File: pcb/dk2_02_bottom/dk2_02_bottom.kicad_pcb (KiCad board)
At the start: 2 copper layers, 120 x 80 mm, 76 parts, among them J1 Conn_01x18_Pin, J2 Conn_01x18_Pin, J3 Eurorack_Power, Q1 MMBT3904, U1 Pico, U2 AP7333-33SRG, U3 TL072, U4 PCM5102, U5 TL072, U6 TL072, U7 TL072, U8 XL1509-5.0

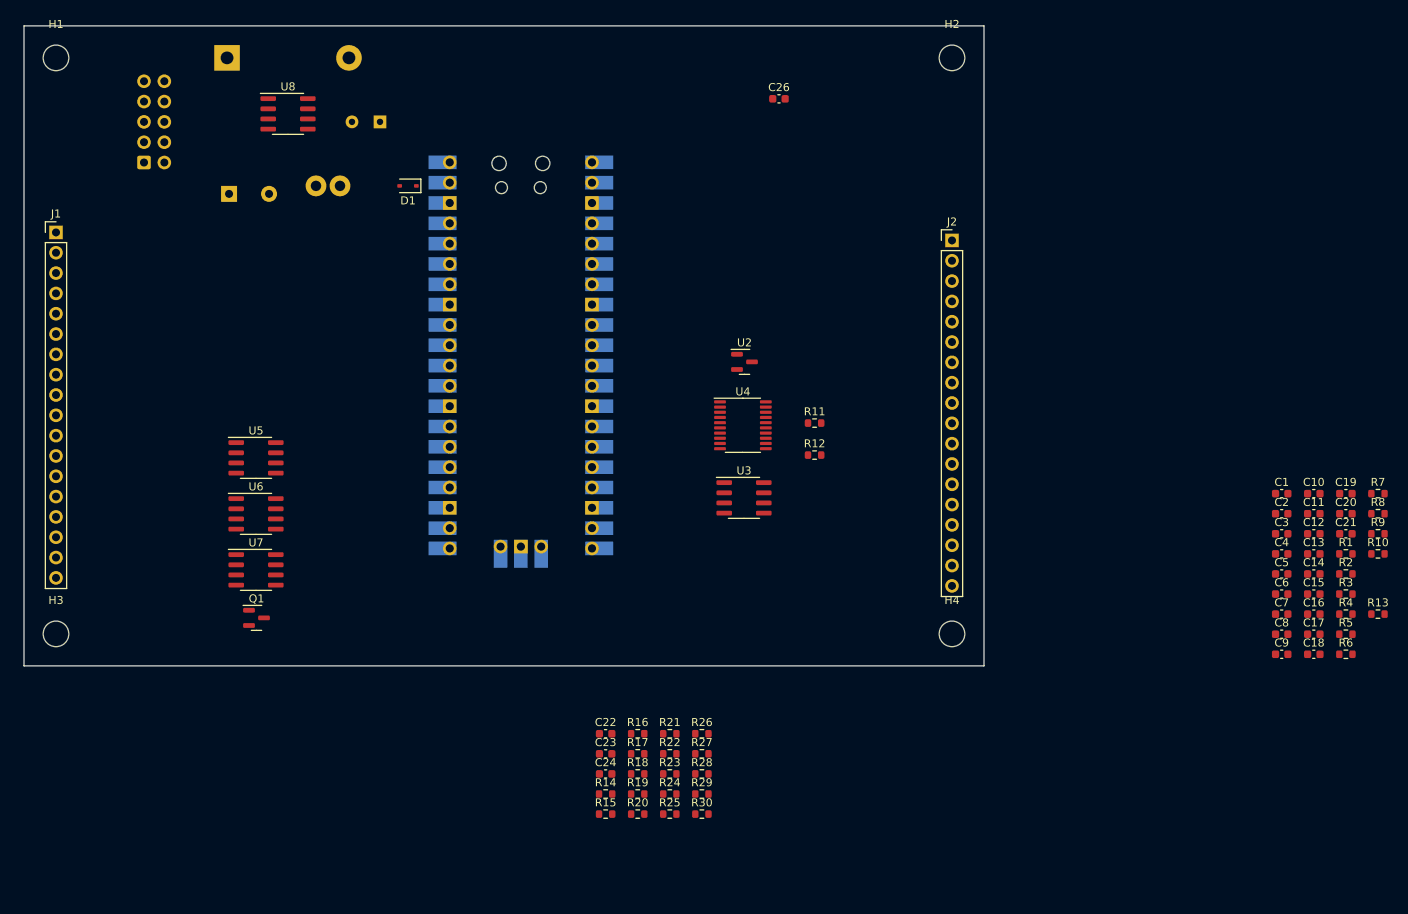
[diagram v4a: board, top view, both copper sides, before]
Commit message: started component placement on bottom board
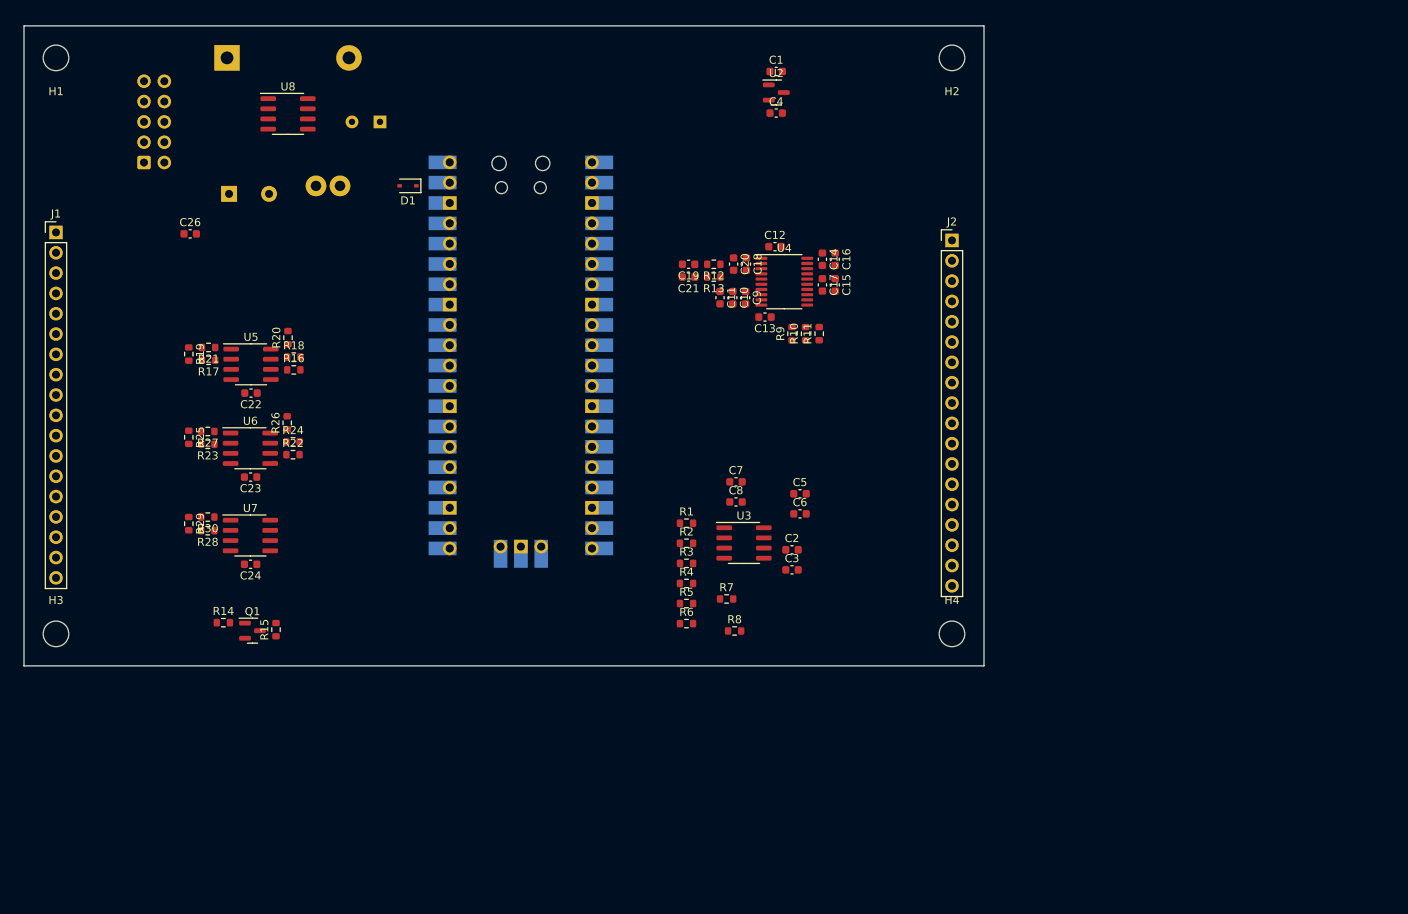
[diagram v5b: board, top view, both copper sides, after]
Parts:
- moved R13 93.1 mm to (166.2, 81.4), turned to 180 degrees
- moved C21 88.2 mm to (163.1, 81.4), turned to 180 degrees
- moved C19 87.0 mm to (163.1, 79.8), turned to 180 degrees
- moved C18 86.1 mm to (170.3, 79.8), turned to -90 degrees
- moved C4 83.8 mm to (174.0, 60.9)
- moved C20 82.7 mm to (168.7, 79.8), turned to -90 degrees
- moved R1 82.5 mm to (162.8, 112.2)
- moved R2 82.5 mm to (162.8, 114.7)
- moved R3 82.5 mm to (162.8, 117.2)
- moved R4 82.5 mm to (162.8, 119.7)
- moved R5 82.5 mm to (162.8, 122.2)
- moved R6 82.5 mm to (162.8, 124.7)
- moved R7 82.5 mm to (167.8, 121.6)
- moved C1 82.3 mm to (174.0, 55.7)
- moved R8 81.7 mm to (168.8, 125.6)
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
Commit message: bottom pcb placement done
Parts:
- moved C26 25.7 mm to (116.8, 55.9), turned to 90 degrees
- moved R6 22.9 mm to (180.3, 110.0), turned to 180 degrees
- moved R8 22.2 mm to (180.3, 106.6)
- moved R7 20.9 mm to (180.3, 104.9)
- moved R4 19.2 mm to (180.3, 111.7), turned to 180 degrees
- moved D2 18.0 mm to (106.5, 72.0), turned to 90 degrees
- moved R2 17.6 mm to (180.3, 113.4), turned to 180 degrees
- moved R5 15.1 mm to (169.6, 108.7)
- moved D1 14.0 mm to (130.2, 56.2)
- moved C25 13.8 mm to (118.1, 65.2), turned to 180 degrees
- moved C8 11.4 mm to (180.3, 108.3), turned to 180 degrees
- moved C2 10.9 mm to (166.3, 110.4)
- moved C3 9.85 mm to (183.6, 111.7), turned to 180 degrees
- moved R3 9.58 mm to (169.6, 110.4)
- moved U8 9.04 mm to (120.5, 56.0), turned to 90 degrees
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
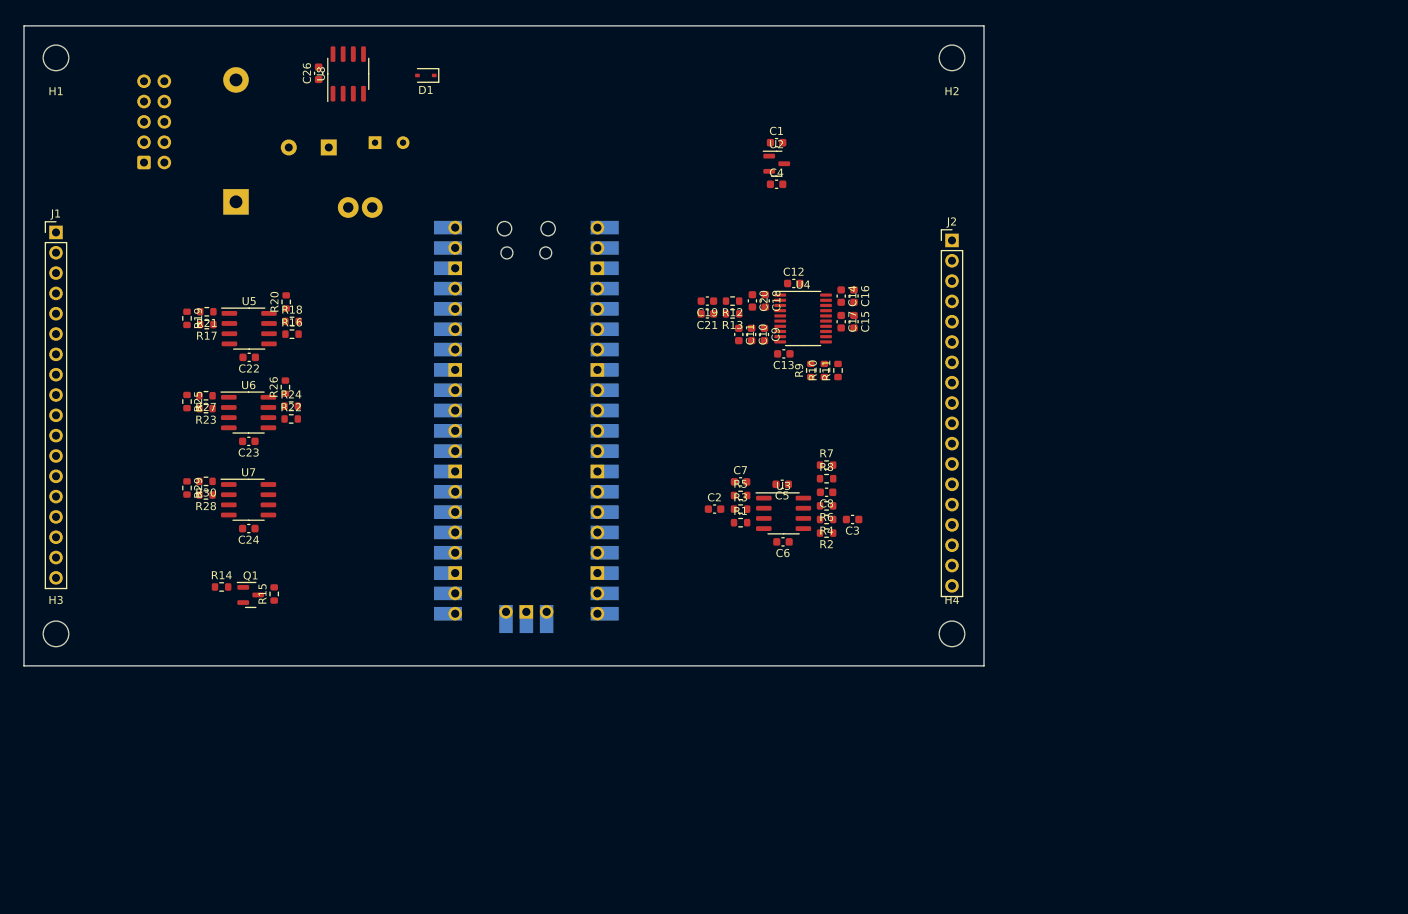
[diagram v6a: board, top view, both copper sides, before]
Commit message: bottom routing mainly done
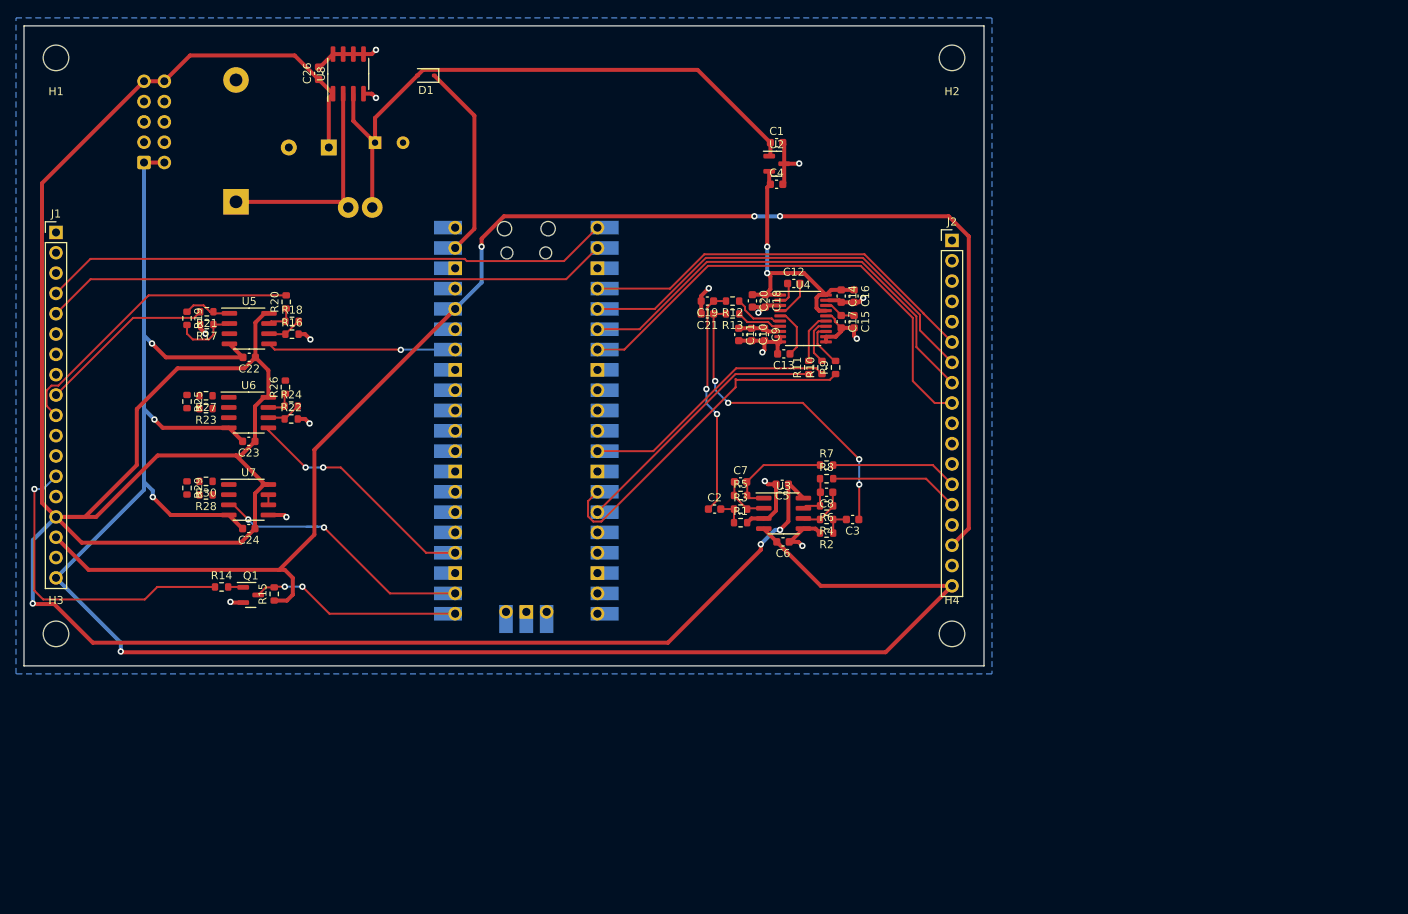
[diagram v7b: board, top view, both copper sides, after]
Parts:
- moved R11 3.67 mm to (178.1, 92.7)
- moved R9 3.12 mm to (181.4, 92.7)
- moved R10 0.48 mm to (179.8, 92.7)
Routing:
- net +12V: track 0.00 -> 340.6 mm, vias 0 -> 3
- net -12V: track 0.00 -> 250.7 mm, vias 0 -> 4
- net +3.3V: track 0.00 -> 190.9 mm, vias 0 -> 3
- net +5V: track 0.00 -> 76.0 mm
- net GND: track 0.00 -> 72.7 mm, vias 0 -> 15
- net START_STOP_BUTTON: track 0.00 -> 71.3 mm
- net TAP_TEMPO_BUTTON: track 0.00 -> 71.1 mm
- net SD_CHIP_SELECT: track 0.00 -> 60.4 mm
- net SD_SERIAL_OUT: track 0.00 -> 56.3 mm
- net SD_SERIAL_IN: track 0.00 -> 53.5 mm
- net SD_CLOCK: track 0.00 -> 50.7 mm
- net DAC_BCLK: track 0.00 -> 43.1 mm
- net +3.3VDAC: track 0.00 -> 40.8 mm, vias 0 -> 2
- net LINE_OUT_R: track 0.00 -> 40.3 mm, vias 0 -> 4
- net SYNC_IN_EURO: track 0.00 -> 39.7 mm, vias 0 -> 1
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- added copper zone on B.Cu, net GND

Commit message: routing done
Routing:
- net 165_LOAD: track 0.00 -> 91.9 mm
- net 4051_ADDRESS_B: track 0.00 -> 91.1 mm, vias 0 -> 1
- net 4051_ADDRESS_A: track 0.00 -> 89.1 mm, vias 0 -> 1
- net 4051_ADDRESS_C: track 0.00 -> 87.5 mm, vias 0 -> 2
- net 165_DATA: track 0.00 -> 85.6 mm, vias 0 -> 3
- net +3.3V: track 190.9 -> 272.8 mm, vias 3 -> 4
- net 165_CLOCK: track 0.00 -> 79.6 mm, vias 0 -> 4
- net 4051_READING_0: track 0.00 -> 78.6 mm, vias 0 -> 2
- net 4051_READING_1: track 0.00 -> 76.3 mm, vias 0 -> 2
- net TRIGGER_OUT_1: track 0.00 -> 63.0 mm, vias 0 -> 2
- net 595_CLOCK: track 0.00 -> 52.7 mm, vias 0 -> 2
- net 595_LATCH: track 0.00 -> 51.8 mm, vias 0 -> 2
- net 595_DATA: track 0.00 -> 50.4 mm, vias 0 -> 2
- net TRIGGER_OUT_4_EURO: track 0.00 -> 37.0 mm, vias 0 -> 2
- net TRIGGER_OUT_3: track 0.00 -> 30.0 mm, vias 0 -> 2
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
